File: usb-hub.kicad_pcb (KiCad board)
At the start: 4 copper layers, 23 x 28.1 mm, 51 parts, among them J1 USB_C_Receptacle_16pin, J2 USB_C_Receptacle_16pin, J3 USB_C_Receptacle_16pin, J4 Conn_01x01_Female, J5 Conn_01x01_Female, J6 Conn_01x01_Female, J7 Conn_01x01_Female, P1 CONN_02X03, Q1 Q_PMOS_GSD 2A, Q2 Q_NMOS_GSD 1Amp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

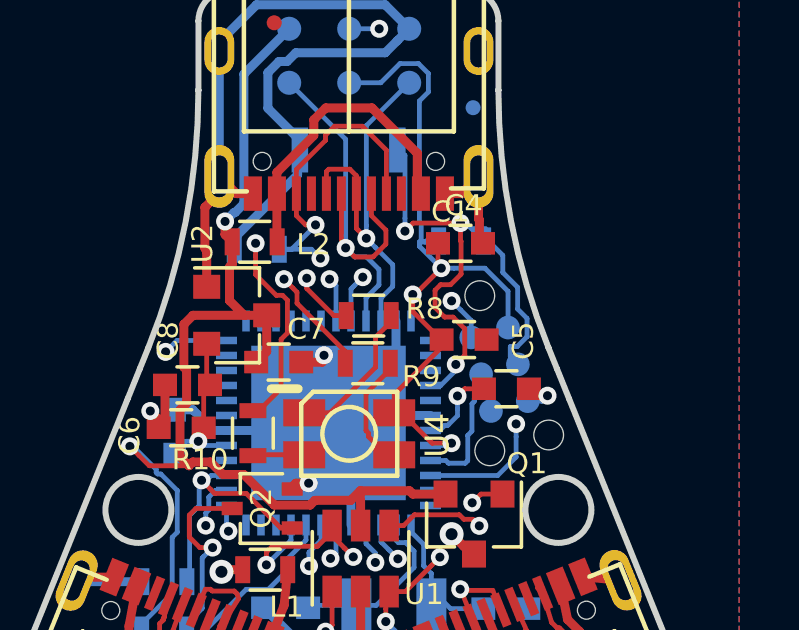
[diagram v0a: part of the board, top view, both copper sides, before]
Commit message: better ground pours
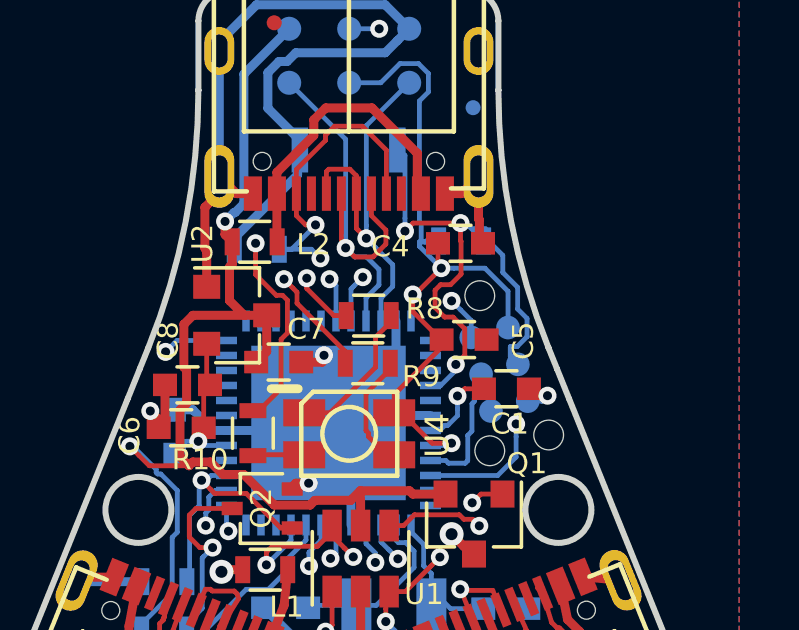
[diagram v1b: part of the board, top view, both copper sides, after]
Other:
- board text removed: "0,80"
- board text removed: "A3"
- board text removed: "BOTTOM VIEW"
- board text removed: "Commentaries:"
- board text removed: "Date"
- board text removed: "Don't put your stuff here!"
- board text removed: "Drowner"
- board text removed: "Manel Senís"
- board text removed: "Milimetres(mm)"
- board text removed: "Name"
- board text removed: "PCB-HUBLE-NEW_2_ASM"
- board text removed: "Page 1 / 1"
- board text removed: "Reference file:"
- board text removed: "Scale:2:1"
- board text removed: "Supplier"
- board text removed: "TOP VIEW"
- board text removed: "TÍTULO / Title:"
- board text removed: "Units"

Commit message: hide many values
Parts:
- C1: value 1uF, ceramic, 6v, 10%, x5r -> e1uF, ceramic, 6v, 10%, x5r
- Y1: value 32.768khz -> e32.768khz

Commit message: fixes for gp
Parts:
- removed R13, R5: 36k, 125mW, 5%, raise_fp:R_0603
- added TP12: TEST, raise_fp:testpoint, B.Cu at (139.0, 116.5)
- added TP9: TEST, raise_fp:testpoint, B.Cu at (146.5, 114.5)
- C1: value e1uF, ceramic, 6v, 10%, x5r -> 1uF, ceramic, 6v, 10%, x5r
- Q1: value Q_PMOS_GSD 2A -> PMOS, -3.6A, 0.02R
- U4: value 4 pin RGB led, com anode, red: 500mcd 620nm. Green: 1000mcd 520nm. Blue: 500mcd 460nm. -> 4 pin RGB led, com anode
- Y1: value e32.768khz -> 32.768khz
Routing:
- net Earth: track 83.9 -> 112.3 mm
- net +3V3: track 75.0 -> 63.4 mm, vias 7 -> 6
- net /sda: track 50.6 -> 54.0 mm, vias 4 -> 5
- net /scl: track 48.2 -> 50.4 mm
- net /dfp-r-cc: track 27.7 -> 26.4 mm
- removed copper zone on B.Cu, net Earth
- removed copper zone on F.Cu, net Earth
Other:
- board text added: "d+ 3.3 d-"
- board text added: "scl"
- board text added: "sda"
- board text removed: "u+ 3.3 u-"

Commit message: led updated to show fp on fab layer
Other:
- board text added: "led"
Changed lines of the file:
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@@
   (general
     (thickness 0.8)
-    (drawings 166)
+    (drawings 173)
     (tracks 808)
     (zones 0)
@@
   )
   (layers
-    (0 F.Cu signal)
-    (1 In1.Cu power)
-    (2 In2.Cu power)
-    (31 B.Cu signal)
+    (0 F.Cu signal hide)
+    (1 In1.Cu power hide)
+    (2 In2.Cu power hide)
+    (31 B.Cu signal hide)
     (32 B.Adhes user)
     (33 F.Adhes user)
@@
   (module raise_fp:reset-button (layer B.Cu)
     (at 141.98 97.24)
+    (attr smd)
     (fp_text reference SW1 (at -3.16 -1.01) (layer B.SilkS)
       (effects (font (size 0.7 0.7) (thickness 0.1)) (justify mirror))
@@
       (net 24 /scl))
   )
+  (gr_line (start 141.6 105.7) (end 142.1 105.7) (layer F.Fab) (width 0.2))
+  (gr_line (start 140.8 106.6) (end 141.6 105.7) (layer F.Fab) (width 0.2))
+  (gr_line (start 140.8 107.9) (end 140.8 106.6) (layer F.Fab) (width 0.2))
+  (gr_line (start 144.1 107.9) (end 140.8 107.9) (layer F.Fab) (width 0.2))
+  (gr_line (start 144.1 105.7) (end 144.1 107.9) (layer F.Fab) (width 0.2))
+  (gr_line (start 142 105.7) (end 144.1 105.7) (layer F.Fab) (width 0.2))
+  (gr_text led (at 142.3 106.7) (layer F.Fab)
+    (effects (font (size 1 1) (thickness 0.25)))
+  )
   (gr_text sda (at 145 115.5 20) (layer B.SilkS)

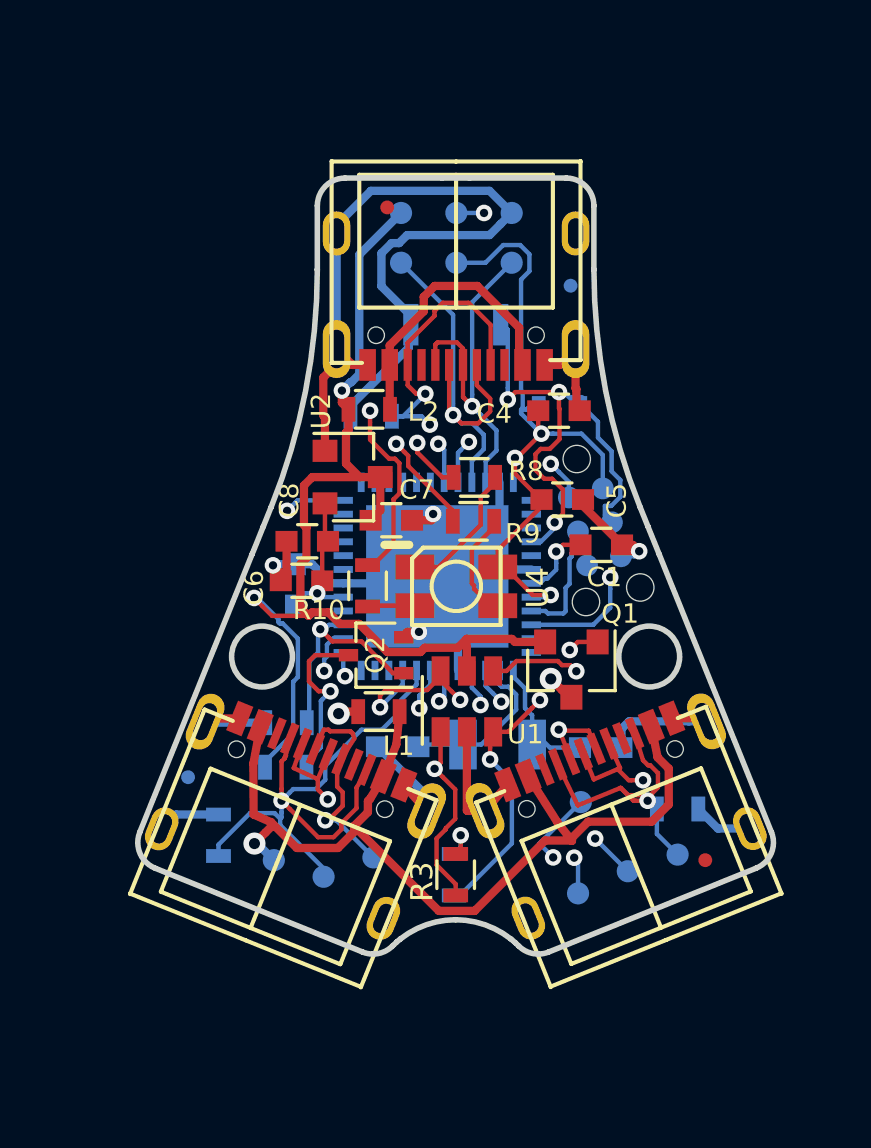
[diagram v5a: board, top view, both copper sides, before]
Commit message: moved sockets in by 1.25mm
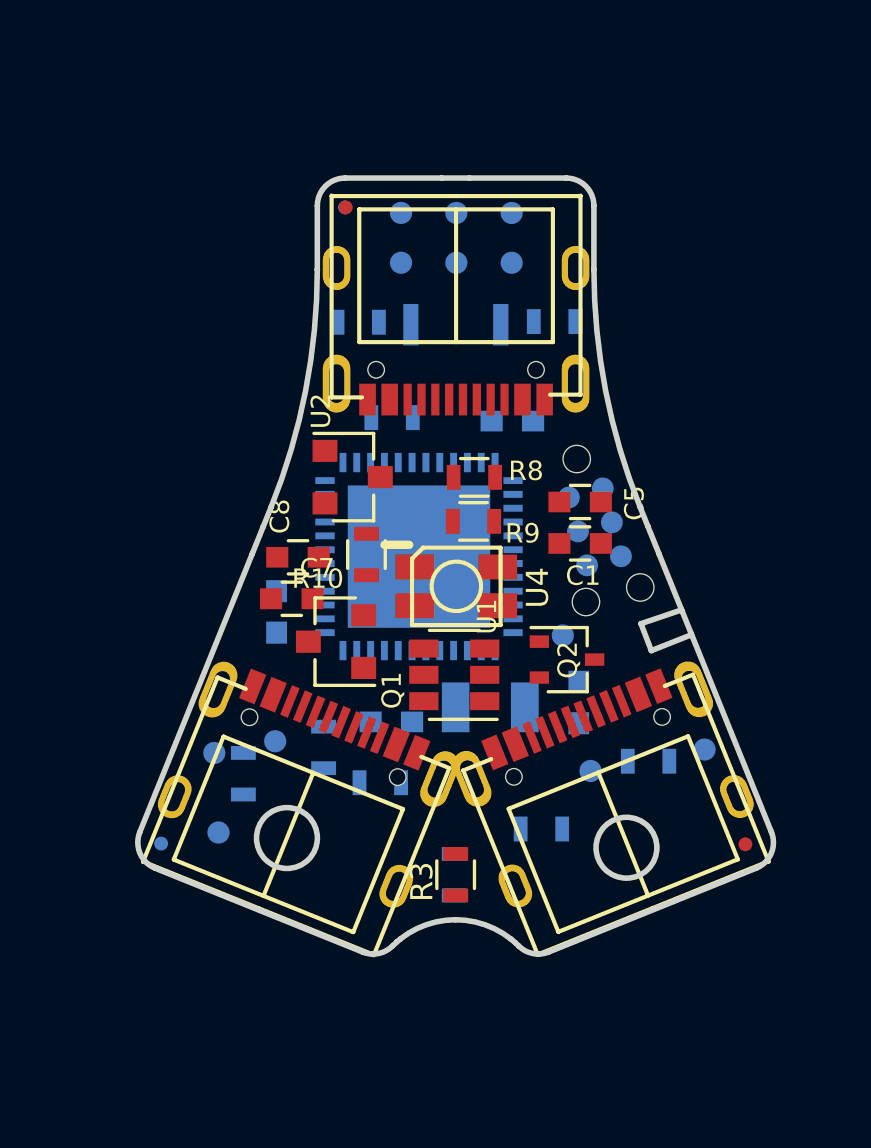
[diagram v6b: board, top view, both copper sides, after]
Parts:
- removed C9: 10uF, ceramic, 6v, 10%, x5r, raise_fp:C_0603
- removed TP11: TEST, raise_fp:testpoint
- C4, C6, L1, L2: moved to B.Cu
- moved TP9 11.3 mm to (135.4, 112.3)
- moved L1 9.91 mm to (148.9, 113.0), turned to 180 degrees
- moved TP10 8.84 mm to (145.8, 108.5)
- moved J4 8.63 mm to (138.0, 93.0)
- moved Q1 8.57 mm to (137.7, 108.7), turned to 180 degrees
- moved TP12 8.45 mm to (146.8, 113.4)
- moved Q2 6.90 mm to (146.0, 109.3), turned to 0 degrees
- moved R11 4.98 mm to (145.1, 115.5)
- moved C7 4.59 mm to (136.1, 107.2)
- moved TP7 4.43 mm to (133.2, 112.7)
- moved TP6 4.12 mm to (133.4, 115.6)
- moved TP2 3.92 mm to (151.0, 112.6)
- moved R1 3.47 mm to (139.2, 113.8)
- moved R6 3.43 mm to (138.4, 97.2)
- moved R7 3.15 mm to (145.6, 97.1)
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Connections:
- U3 pad 3: Net-(TP10-Pad1) -> Net-(U3-Pad3)
- U3 pad 47: Net-(U3-Pad47) -> Net-(TP10-Pad1)
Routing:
- net Earth: track 112.3 -> 0.00 mm, vias 4 -> 0
- net +3V3: track 63.4 -> 0.00 mm, vias 6 -> 0
- net /sda: track 54.0 -> 0.00 mm, vias 5 -> 0
- net /scl: track 50.4 -> 0.00 mm, vias 5 -> 0
- net /dfp-l-cc: track 48.3 -> 0.00 mm, vias 2 -> 0
- net +5V: track 40.8 -> 0.00 mm, vias 2 -> 0
- net /side-power: track 34.6 -> 0.00 mm, vias 1 -> 0
- net /ufp-cc: track 32.1 -> 0.00 mm, vias 4 -> 0
- net /dfp-r-cc: track 26.4 -> 0.00 mm, vias 3 -> 0
- net /reset: track 18.7 -> 0.00 mm, vias 3 -> 0
- net Net-(Q1-Pad1): track 16.7 -> 0.00 mm, vias 2 -> 0
- net /usb-up_N: track 15.0 -> 0.00 mm, vias 1 -> 0
- net /pwm1_r: track 14.8 -> 0.00 mm, vias 2 -> 0
- net /pwm1_b: track 13.8 -> 0.00 mm, vias 2 -> 0
- net /pwm1_g: track 13.7 -> 0.00 mm, vias 2 -> 0
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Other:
- outline, holes or cut-outs redrawn

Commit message: moving sockets
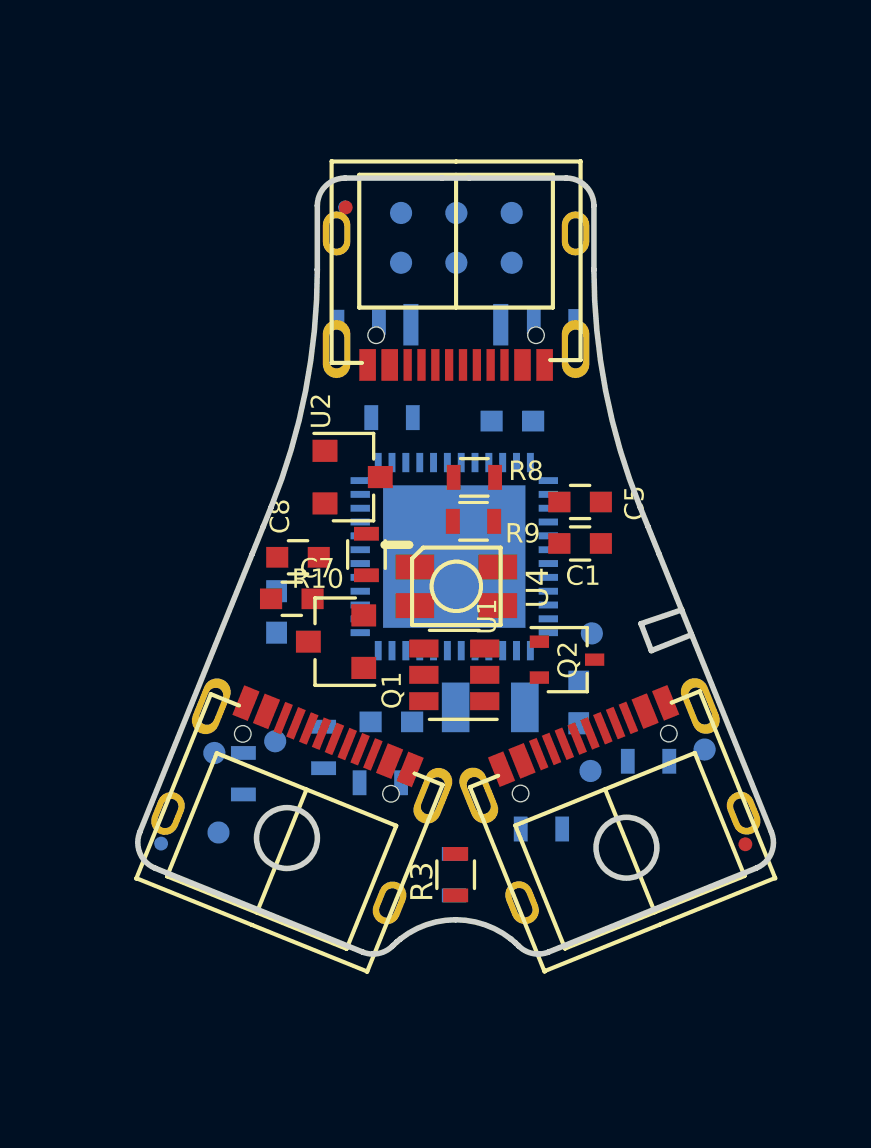
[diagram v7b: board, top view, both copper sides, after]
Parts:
- removed P1: CONN_02X03, raise_fp:Tag-Connect_TC2030-IDC-NL
- moved U3 1.28 mm to (141.9, 105.6)
- moved J1 1.25 mm to (142.0, 98.1)
- moved TP10 1.05 mm to (146.9, 108.4)
- moved J2 0.65 mm to (137.1, 112.7)
- moved J3 0.65 mm to (146.8, 112.6)

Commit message: replaced programming header with test pads
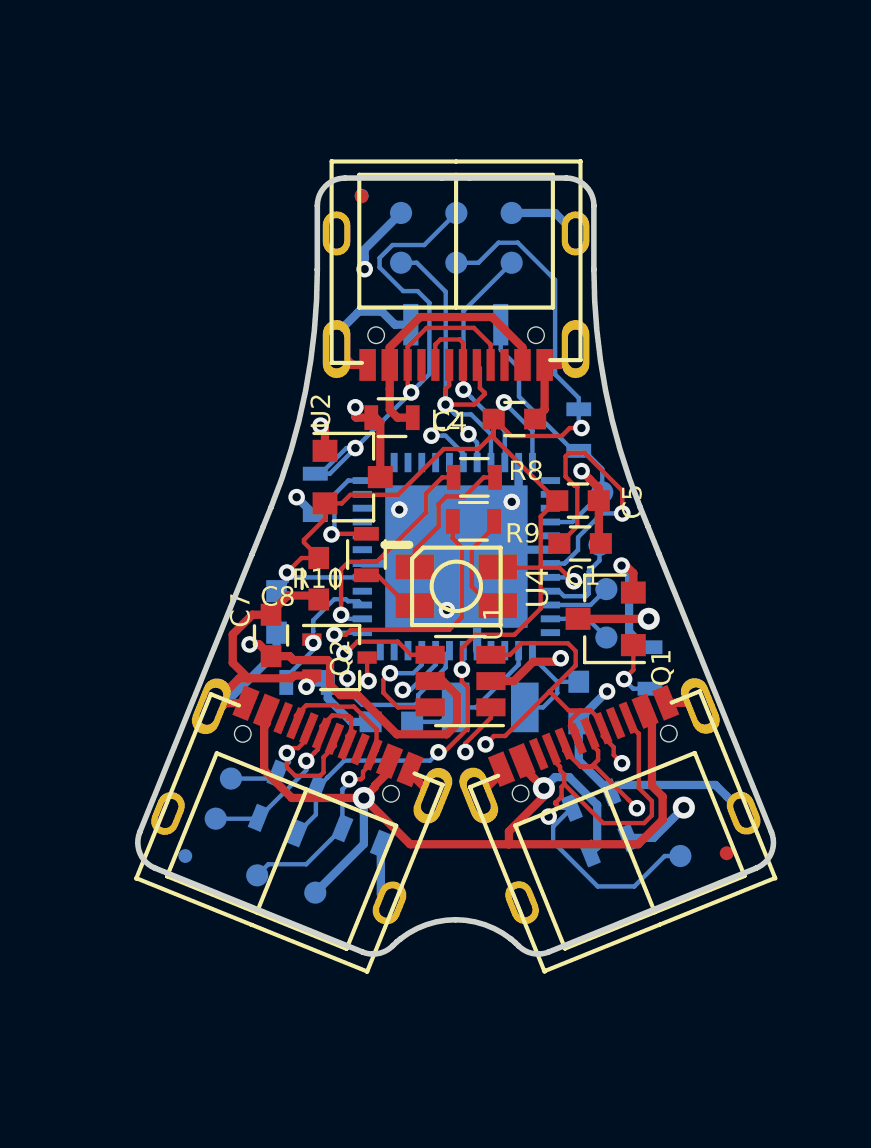
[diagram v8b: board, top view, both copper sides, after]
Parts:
- added TP11: TEST, raise_fp:testpoint, B.Cu at (147.4, 106.8)
- added TP14: TEST, raise_fp:testpoint, B.Cu at (147.2, 105.2)
- added TP15: TEST, raise_fp:testpoint, B.Cu at (147.3, 103.3)
- C4, L2: moved to F.Cu
- R3: moved to B.Cu
- moved TP12 13.7 mm to (133.3, 115.1)
- moved R1 10.6 mm to (149.0, 109.7), turned to 270 degrees
- moved Q1 9.78 mm to (147.4, 107.9)
- moved Q2 8.23 mm to (137.8, 109.3)
- moved R3 6.67 mm to (136.2, 113.8), turned to 338 degrees
- moved R4 6.62 mm to (135.6, 115.3), turned to 338 degrees
- moved R6 6.42 mm to (136.9, 103.4), turned to 270 degrees
- moved TP7 6.23 mm to (136.9, 117.8)
- moved R12 4.83 mm to (138.6, 115.7), turned to 338 degrees
- moved R7 4.02 mm to (146.4, 101.0), turned to 90 degrees
- moved TP2 3.95 mm to (150.1, 116.5)
- moved L1 3.37 mm to (147.5, 116.1), turned to 202 degrees
- moved R2 2.43 mm to (136.6, 110.2), turned to 0 degrees
- moved TP9 2.09 mm to (133.8, 113.7)
- moved TP6 2.09 mm to (134.8, 117.2)
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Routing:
- net Earth: track 0.00 -> 78.1 mm, vias 0 -> 9
- net +3V3: track 0.00 -> 59.6 mm, vias 0 -> 6
- net +5V: track 0.00 -> 53.9 mm, vias 0 -> 4
- net /sda: track 0.00 -> 52.8 mm, vias 0 -> 4
- net /scl: track 0.00 -> 48.3 mm, vias 0 -> 4
- net /side-power: track 0.00 -> 36.3 mm, vias 0 -> 2
- net /ufp-cc: track 0.00 -> 36.1 mm, vias 0 -> 3
- net /dfp-r-cc: track 0.00 -> 34.5 mm, vias 0 -> 2
- net Net-(Q1-Pad1): track 0.00 -> 27.6 mm, vias 0 -> 2
- net /dfp-l-cc: track 0.00 -> 25.1 mm, vias 0 -> 3
- net /usb-up_N: track 0.00 -> 13.5 mm, vias 0 -> 1
- net Net-(L1-Pad1): track 0.00 -> 12.4 mm, vias 0 -> 2
- net /usb-up_P: track 0.00 -> 12.1 mm, vias 0 -> 1
- net Net-(C1-Pad2): track 0.00 -> 10.7 mm, vias 0 -> 1
- net /reset: track 0.00 -> 10.1 mm
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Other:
- outline, holes or cut-outs redrawn
